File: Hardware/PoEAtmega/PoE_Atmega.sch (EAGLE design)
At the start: 58 parts, among them IC2 ATMEGA32U4-MU, U1 ARDUINOR3-BPLACE, U2 SPX3819-3.3, U4 W5500, X1 J1011F21P, X3 microUSB, Y2 CRYSTAL-GROUNDEDSMD-3.2X2.5, Y4 8MHz

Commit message: routed but need to meet DRC
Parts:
- removed D1: MBR120, microbuilder:DIODE-SCHOTTKYSOD-123
- removed R9: 100k, microbuilder:RESISTOR0603MINI
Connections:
- net EN: no longer R9.2, U2.EN
- net VBAT: no longer C1.2, C2.+, R6.2, U$1.+VDC
- net VBUS: now also C1.2, C2.+, R6.2, U$1.+VDC, U2.EN; no longer R9.1
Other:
- moved on the sheet: IC2
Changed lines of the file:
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@@
 <grid distance="0.1" unitdist="inch" unit="inch" style="lines" multiple="1" display="no" altdistance="0.01" altunitdist="inch" altunit="inch"/>
 <layers>
-<layer number="1" name="Top" color="4" fill="1" visible="no" active="no"/>
-<layer number="16" name="Bottom" color="1" fill="1" visible="no" active="no"/>
-<layer number="17" name="Pads" color="2" fill="1" visible="no" active="no"/>
-<layer number="18" name="Vias" color="2" fill="1" visible="no" active="no"/>
-<layer number="19" name="Unrouted" color="6" fill="1" visible="no" active="no"/>
-<layer number="20" name="Dimension" color="24" fill="1" visible="no" active="no"/>
-<layer number="21" name="tPlace" color="7" fill="1" visible="no" active="no"/>
-<layer number="22" name="bPlace" color="7" fill="1" visible="no" active="no"/>
-<layer number="23" name="tOrigins" color="15" fill="1" visible="no" active="no"/>
-<layer number="24" name="bOrigins" color="15" fill="1" visible="no" active="no"/>
-<layer number="25" name="tNames" color="7" fill="1" visible="no" active="no"/>
-<layer number="26" name="bNames" color="7" fill="1" visible="no" active="no"/>
-<layer number="27" name="tValues" color="7" fill="1" visible="no" active="no"/>
-<layer number="28" name="bValues" color="7" fill="1" visible="no" active="no"/>
+<layer number="1" name="Top" color="4" fill="1" visible="yes" active="no"/>
+<layer number="16" name="Bottom" color="1" fill="1" visible="yes" active="no"/>
+<layer number="17" name="Pads" color="2" fill="1" visible="yes" active="no"/>
+<layer number="18" name="Vias" color="2" fill="1" visible="yes" active="no"/>
+<layer number="19" name="Unrouted" color="6" fill="1" visible="yes" active="no"/>
+<layer number="20" name="Dimension" color="24" fill="1" visible="yes" active="no"/>
+<layer number="21" name="tPlace" color="7" fill="1" visible="yes" active="no"/>
+<layer number="22" name="bPlace" color="7" fill="1" visible="yes" active="no"/>
+<layer number="23" name="tOrigins" color="15" fill="1" visible="yes" active="no"/>
+<layer number="24" name="bOrigins" color="15" fill="1" visible="yes" active="no"/>
+<layer number="25" name="tNames" color="7" fill="1" visible="yes" active="no"/>
+<layer number="26" name="bNames" color="7" fill="1" visible="yes" active="no"/>
+<layer number="27" name="tValues" color="7" fill="1" visible="yes" active="no"/>
+<layer number="28" name="bValues" color="7" fill="1" visible="yes" active="no"/>
 <layer number="29" name="tStop" color="7" fill="3" visible="no" active="no"/>
 <layer number="30" name="bStop" color="7" fill="6" visible="no" active="no"/>
@@
 <layer number="35" name="tGlue" color="7" fill="4" visible="no" active="no"/>
 <layer number="36" name="bGlue" color="7" fill="5" visible="no" active="no"/>
-<layer number="37" name="tTest" color="7" fill="1" visible="no" active="no"/>
-<layer number="38" name="bTest" color="7" fill="1" visible="no" active="no"/>
+<layer number="37" name="tTest" color="7" fill="1" visible="yes" active="no"/>
+<layer number="38" name="bTest" color="7" fill="1" visible="yes" active="no"/>
 <layer number="39" name="tKeepout" color="4" fill="11" visible="no" active="no"/>
 <layer number="40" name="bKeepout" color="1" fill="11" visible="no" active="no"/>
@@
 <layer number="44" name="Drills" color="7" fill="1" visible="no" active="no"/>
 <layer number="45" name="Holes" color="7" fill="1" visible="no" active="no"/>
-<layer number="46" name="Milling" color="3" fill="1" visible="no" active="no"/>
-<layer number="47" name="Measures" color="7" fill="1" visible="no" active="no"/>
-<layer number="48" name="Document" color="7" fill="1" visible="no" active="no"/>
-<layer number="49" name="Reference" color="7" fill="1" visible="no" active="no"/>
-<layer number="50" name="dxf" color="7" fill="1" visible="no" active="no"/>
-<layer number="51" name="tDocu" color="7" fill="1" visible="no" active="no"/>
-<layer number="52" name="bDocu" color="7" fill="1" visible="no" active="no"/>
-<layer number="53" name="tGND_GNDA" color="7" fill="9" visible="no" active="no"/>
-<layer number="54" name="bGND_GNDA" color="1" fill="9" visible="no" active="no"/>
-<layer number="56" name="wert" color="7" fill="1" visible="no" active="no"/>
-<layer number="57" name="tCAD" color="7" fill="1" visible="no" active="no"/>
-<layer number="59" name="tCarbon" color="7" fill="1" visible="no" active="no"/>
-<layer number="60" name="bCarbon" color="7" fill="1" visible="no" active="no"/>
+<layer number="46" name="Milling" color="3" fill="1" visible="yes" active="no"/>
+<layer number="47" name="Measures" color="7" fill="1" visible="yes" active="no"/>
+<layer number="48" name="Document" color="7" fill="1" visible="yes" active="no"/>
+<layer number="49" name="Reference" color="7" fill="1" visible="yes" active="no"/>
+<layer number="50" name="dxf" color="7" fill="1" visible="yes" active="no"/>
+<layer number="51" name="tDocu" color="7" fill="1" visible="yes" active="no"/>
+<layer number="52" name="bDocu" color="7" fill="1" visible="yes" active="no"/>
+<layer number="53" name="tGND_GNDA" color="7" fill="9" visible="yes" active="no"/>
+<layer number="54" name="bGND_GNDA" color="1" fill="9" visible="yes" active="no"/>
+<layer number="56" name="wert" color="7" fill="1" visible="yes" active="no"/>
+<layer number="57" name="tCAD" color="7" fill="1" visible="yes" active="no"/>
+<layer number="59" name="tCarbon" color="7" fill="1" visible="yes" active="no"/>
+<layer number="60" name="bCarbon" color="7" fill="1" visible="yes" active="no"/>
 <layer number="90" name="Modules" color="5" fill="1" visible="yes" active="yes"/>
 <layer number="91" name="Nets" color="2" fill="1" visible="yes" active="yes"/>
@@
 <part name="U$21" library="microbuilder" deviceset="VBAT" device=""/>
 <part name="U2" library="microbuilder" deviceset="VREG_SOT23-5" device="" value="SPX3819-3.3"/>
-<part name="R9" library="microbuilder" deviceset="RESISTOR" device="0603MINI" value="100k"/>
 <part name="U$4" library="microbuilder" deviceset="VBAT" device=""/>
 <part name="JP5" library="microbuilder" deviceset="HEADER-1X14" device=""/>
@@
 <part name="H2" library="holes" deviceset="MOUNT-HOLE" device="3.2"/>
 <part name="H3" library="holes" deviceset="MOUNT-HOLE" device="3.2"/>
-<part name="D1" library="microbuilder" deviceset="DIODE-SCHOTTKY" device="SOD-123" value="MBR120"/>
 <part name="R6" library="microbuilder" deviceset="RESISTOR" device="2512" value="27 Ohm"/>
 <part name="+3V5" library="supply1" deviceset="+3V3" device=""/>
@@
 <instance part="U$21" gate="G$1" x="25.4" y="259.08"/>
 <instance part="U2" gate="G$1" x="48.26" y="238.76"/>
-<instance part="R9" gate="G$1" x="30.48" y="238.76"/>
 <instance part="U$4" gate="G$1" x="111.76" y="66.04"/>
 <instance part="JP5" gate="G$1" x="447.04" y="218.44"/>
@@
 <instance part="H2" gate="G$1" x="386.08" y="101.6"/>
 <instance part="H3" gate="G$1" x="386.08" y="86.36"/>
-<instance part="D1" gate="G$1" x="33.02" y="251.46" rot="R270"/>
 <instance part="R6" gate="G$1" x="111.76" y="58.42" rot="R90"/>
 <instance part="+3V5" gate="G$1" x="63.5" y="93.98" rot="MR0"/>
@@
 <wire x1="38.1" y1="241.3" x2="25.4" y2="241.3" width="0.1524" layer="91"/>
 <wire x1="25.4" y1="241.3" x2="25.4" y2="238.76" width="0.1524" layer="91"/>
+<pinref part="U2" gate="G$1" pin="IN"/>
 <wire x1="25.4" y1="238.76" x2="25.4" y2="233.68" width="0.1524" layer="91"/>
-<pinref part="U2" gate="G$1" pin="IN"/>
 <wire x1="17.78" y1="241.3" x2="25.4" y2="241.3" width="0.1524" layer="91"/>
-<pinref part="R9" gate="G$1" pin="1"/>
+<wire x1="25.4" y1="256.54" x2="25.4" y2="241.3" width="0.1524" layer="91"/>
+<pinref part="U2" gate="G$1" pin="EN"/>
+<label x="35.56" y="238.76" size="1.778" layer="95" rot="R270"/>
+<wire x1="38.1" y1="238.76" x2="25.4" y2="238.76" width="0.1524" layer="91"/>
 <junction x="25.4" y="238.76"/>
-<wire x1="25.4" y1="256.54" x2="25.4" y2="241.3" width="0.1524" layer="91"/>
-</segment>
-</net>
-<net name="VBAT" class="0">
-<segment>
-<pinref part="U$20" gate="G$1" pin="VBAT"/>
-<wire x1="220.98" y1="246.38" x2="236.22" y2="246.38" width="0.1524" layer="91"/>
-<pinref part="JP3" gate="G$1" pin="1"/>
 </segment>
 <segment>
@@
 </segment>
 </net>
+<net name="VBAT" class="0">
+<segment>
+<pinref part="U$20" gate="G$1" pin="VBAT"/>
+<wire x1="220.98" y1="246.38" x2="236.22" y2="246.38" width="0.1524" layer="91"/>
+<pinref part="JP3" gate="G$1" pin="1"/>
+</segment>
+</net>
 <net name="13" class="0">
 <segment>
@@
 <label x="226.06" y="243.84" size="1.778" layer="95"/>
 </segment>
-<segment>
-<pinref part="U2" gate="G$1" pin="EN"/>
-<pinref part="R9" gate="G$1" pin="2"/>
-<wire x1="35.56" y1="238.76" x2="38.1" y2="238.76" width="0.1524" layer="91"/>
-<label x="35.56" y="238.76" size="1.778" layer="95" rot="R270"/>
-</segment>
-</net>
+</net>

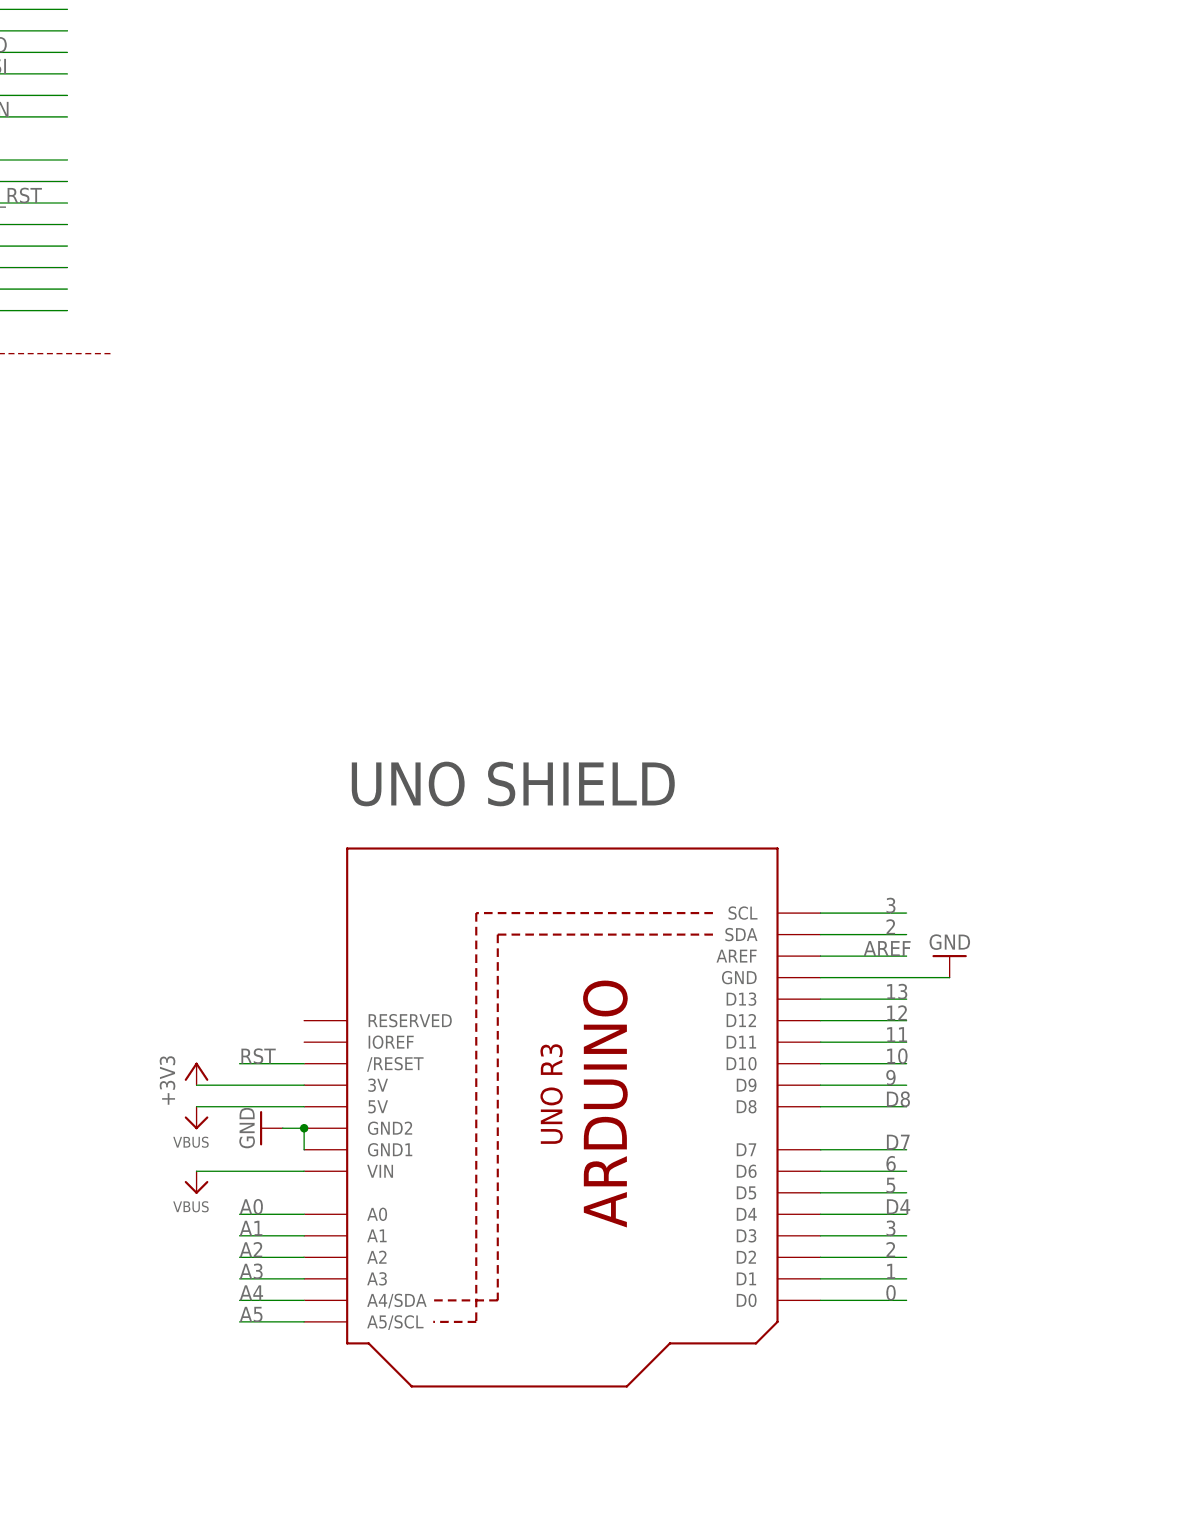
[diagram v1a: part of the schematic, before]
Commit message: HEEP-508 replaced package, need to route ICSP header
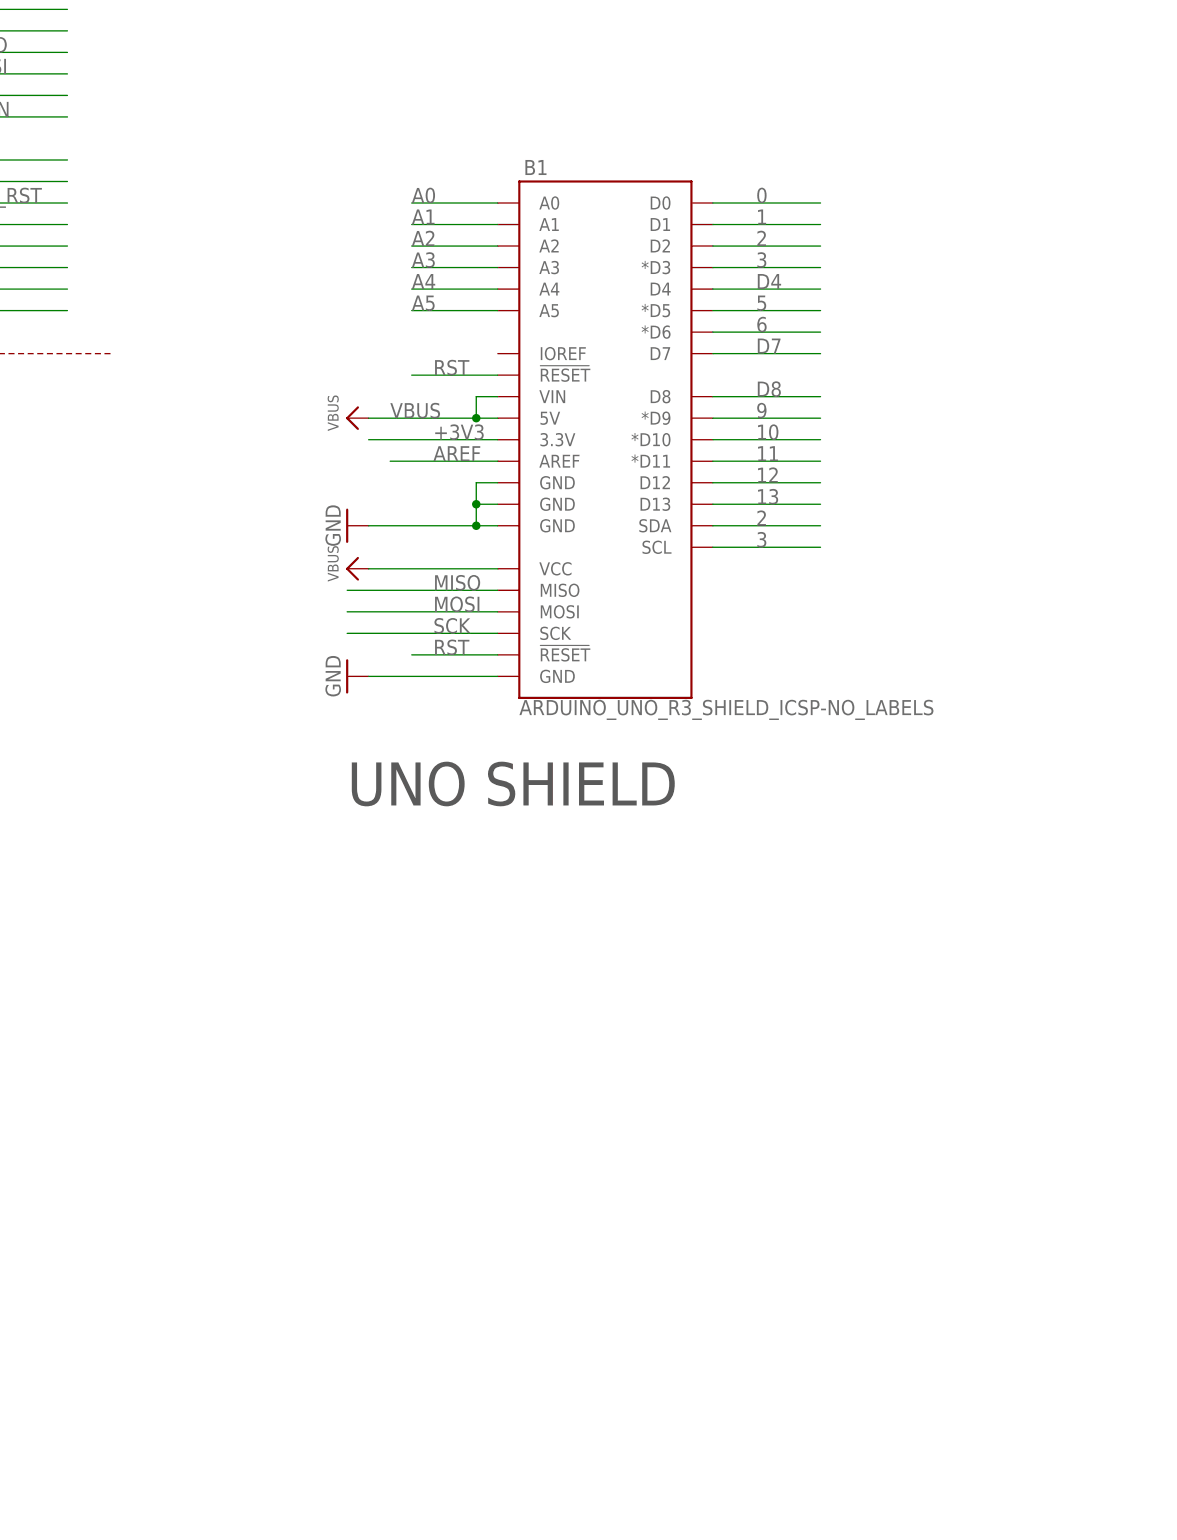
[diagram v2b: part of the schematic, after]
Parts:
- removed U1: ARDUINOR3-BPLACE, adafruit:ARDUINOR3-BPLACE
- added B1: ARDUINO_UNO_R3_SHIELD_ICSP-NO_LABELS, SparkFun-Boards:ARDUINO_UNO_R3_SHIELD_ICSP-NO_LABELS
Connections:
- net +3V3: now also B1.3.3V; no longer U1.3V
- net 0: now also B1.D0; no longer U1.D0
- net 1: now also B1.D1; no longer U1.D1
- net 10: now also B1.*D10; no longer U1.D10
- net 11: now also B1.*D11; no longer U1.D11
- net 12: now also B1.D12; no longer U1.D12
- net 13: now also B1.D13; no longer U1.D13
- net 2: now also B1.D2, B1.SDA; no longer U1.D2, U1.SDA
- net 3: now also B1.*D3, B1.SCL; no longer U1.D3, U1.SCL
- net 5: now also B1.*D5; no longer U1.D5
- net 6: now also B1.*D6; no longer U1.D6
- net 9: now also B1.*D9; no longer U1.D9
- net A0: now also B1.A0; no longer U1.A0
- net A1: now also B1.A1; no longer U1.A1
- net A2: now also B1.A2; no longer U1.A2
- net A3: now also B1.A3; no longer U1.A3
- net A4: now also B1.A4; no longer U1.A4/SDA
- net A5: now also B1.A5; no longer U1.A5/SCL
- net AREF: now also B1.AREF; no longer U1.AREF
- net D4: now also B1.D4; no longer U1.D4
- net D7: now also B1.D7; no longer U1.D7
- net D8: now also B1.D8; no longer U1.D8
- net GND: now also B1.GND, B1.GND@0, B1.GND@1, B1.GND@2; no longer U1.GND, U1.GND1, U1.GND2
- net MISO: now also B1.MISO
- net MOSI: now also B1.MOSI
- net RST: now also B1.!RESET!@1, B1.!RESET!@2; no longer U1./RESET
- net SCK: now also B1.SCK
- net VBUS: now also B1.5V, B1.VCC, B1.VIN; no longer U1.5V, U1.VIN

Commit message: HEEP-508 rdy for dylan review
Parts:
- removed JP2, JP5: (no value), microbuilder:HEADER-1X14
- removed JP4: (no value), microbuilder:HEADER-1X18
- added J1, J2, J5, J6: (no value), SparkFun-Connectors:CONN_18
- added J3, J4: (no value), SparkFun-Connectors:CONN_10"
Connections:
- net 0: now also J5.1, J6.1
- net 1: now also J5.3, J6.3
- net 10: now also J3.3, J4.3
- net 11: now also J3.5, J4.5
- net 12: now also J3.7, J4.7
- net 13: now also J3.9, J4.9
- net 2: now also J5.5, J6.5
- net 3: now also J5.7, J6.7
- net 5: now also J5.11, J6.11
- net 6: now also J5.13, J6.13
- net 9: now also J3.1, J4.1
- net A0: now also J1.17, J2.17
- net A1: now also J1.14, J2.14
- net A2: now also J1.11, J2.11
- net A3: now also J1.8, J2.8
- net A4: now also J1.5, J2.5
- net A5: now also J1.2, J2.2
- net D4: now also J5.9, J6.9
- net D7: now also J5.15, J6.15
- net D8: now also J5.17, J6.17
- net GND: now also J1.12, J1.15, J1.18, J1.3, J1.6, J1.9, J2.12, J2.15, J2.18, J2.3, J2.6, J2.9, J3.10, J3.2, J3.4, J3.6, J3.8, J4.10, J4.2, J4.4, J4.6, J4.8, J5.10, J5.12, J5.14, J5.16, J5.18, J5.2, J5.4, J5.6, J5.8, J6.10, J6.12, J6.14, J6.16, J6.18, J6.2, J6.4, J6.6, J6.8
- net VCC-ISO: now also J1.1, J1.10, J1.13, J1.16, J1.4, J1.7, J2.1, J2.10, J2.13, J2.16, J2.4, J2.7
